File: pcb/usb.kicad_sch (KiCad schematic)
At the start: 31 parts, among them J2 USB_C_Receptacle_USB2.0_16P, Q1 FDN340P, Q2 FS8025A, Q3 FDN340P, SW2 SW_SPST, U2 TP4056-42-ESOP8, U3 DW01A

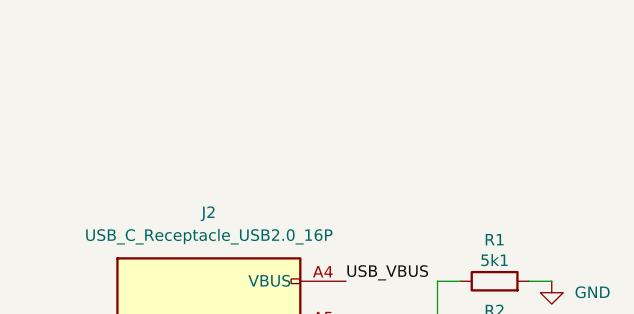
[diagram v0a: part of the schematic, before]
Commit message: Started routing...
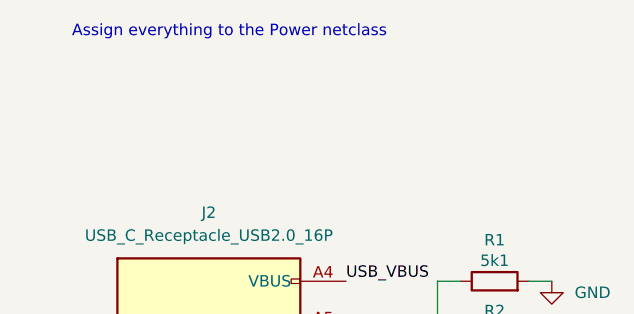
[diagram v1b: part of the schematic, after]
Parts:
- C17, C18: footprint Capacitor_SMD:C_0603_1608Metric_Pad1.08x0.95mm_HandSolder -> Capacitor_SMD:C_0805_2012Metric_Pad1.18x1.45mm_HandSolder
- R4, R5: footprint Resistor_SMD:R_0603_1608Metric_Pad0.98x0.95mm_HandSolder -> Resistor_SMD:R_0805_2012Metric_Pad1.20x1.40mm_HandSolder
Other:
- note added: "Assign everything to the Power netclass"
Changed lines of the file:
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@@
 		)
 	)
+	(text "Assign everything to the Power netclass"
+		(exclude_from_sim no)
+		(at 44.196 20.574 0)
+		(effects
+			(font
+				(size 1.27 1.27)
+			)
+		)
+	)
 	(text "18650 + protection IC"
 		(exclude_from_sim no)
@@
 		)
 	)
+	(rule_area
+		(exclude_from_sim no)
+		(in_bom yes)
+		(on_board yes)
+		(dnp no)
+		(polyline
+			(pts
+				(xy 278.13 163.83) (xy 167.64 163.83) (xy 167.64 195.58) (xy 104.14 195.58) (xy 104.14 101.6) (xy 96.52 93.98)
+				(xy 22.86 93.98) (xy 22.86 17.78) (xy 222.25 17.78) (xy 278.13 73.66)
+			)
+			(stroke
+				(width 0)
+				(type dash)
+			)
+			(fill
+				(type none)
+			)
+		)
+	)
+	(netclass_flag ""
+		(length 2.54)
+		(shape round)
+		(at 31.75 17.78 0)
+		(fields_autoplaced yes)
+		(effects
+			(font
+				(size 1.27 1.27)
+			)
+			(justify left bottom)
+		)
+		(property "Netclass" "Power"
+			(at 32.4485 15.24 0)
+			(show_name no)
+			(do_not_autoplace no)
+			(effects
+				(font
+					(size 1.27 1.27)
+				)
+				(justify left)
+			)
+		)
+		(property "Component Class" ""
+			(at 195.58 59.69 0)
+			(show_name no)
+			(do_not_autoplace no)
+			(effects
+				(font
+					(size 1.27 1.27)
+					(italic yes)
+				)
+			)
+		)
+	)
 	(symbol
 		(lib_id "Battery_Management:DW01A")
@@
 			)
 		)
-		(property "Footprint" "Resistor_SMD:R_0603_1608Metric_Pad0.98x0.95mm_HandSolder"
+		(property "Footprint" "Resistor_SMD:R_0805_2012Metric_Pad1.20x1.40mm_HandSolder"
 			(at 136.652 60.96 90)
 			(hide yes)
@@
 			)
 		)
-		(property "Footprint" "Capacitor_SMD:C_0603_1608Metric_Pad1.08x0.95mm_HandSolder"
+		(property "Footprint" "Capacitor_SMD:C_0805_2012Metric_Pad1.18x1.45mm_HandSolder"
 			(at 126.6952 45.72 0)
 			(hide yes)
@@
 			)
 		)
-		(property "Footprint" "Resistor_SMD:R_0603_1608Metric_Pad0.98x0.95mm_HandSolder"
+		(property "Footprint" "Resistor_SMD:R_0805_2012Metric_Pad1.20x1.40mm_HandSolder"
 			(at 146.812 60.96 90)
 			(hide yes)
@@
 			)
 		)
-		(property "Footprint" "Capacitor_SMD:C_0603_1608Metric_Pad1.08x0.95mm_HandSolder"
+		(property "Footprint" "Capacitor_SMD:C_0805_2012Metric_Pad1.18x1.45mm_HandSolder"
 			(at 220.6752 125.73 0)
 			(hide yes)
